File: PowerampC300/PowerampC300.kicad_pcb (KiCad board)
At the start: 2 copper layers, 240 x 63 mm, 110 parts, among them J1 Conn_01x02, J2 Conn_01x02, J3 Conn_01x02, J4 Conn_01x01, J5 Conn_01x01, J6 Conn_01x01, J7 Conn_01x01, J8 Conn_01x02, J9 Conn_Coaxial, Q1 2N5551, Q10 MJE15033, Q11 MJE15032, Q12 MJE15032, Q13 2N5551, Q14 2N5401, Q15 MJE15032, Q16 MJE15033, Q17 MJL3281A, Q18 MJL1302A, Q19 MJL3281A, Q2 2N5551, Q20 MJL1302A, Q21 MJL3281A, Q22 MJL1302A, Q23 MJL3281A, Q24 MJL1302A, Q3 2N5401, Q4 2N5401, Q5 2N5551, Q6 2N5551, Q7 2N5551, Q8 2N5401

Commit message: Added instructions
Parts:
- moved R24 21.4 mm to (186.2, 76.2)
- moved R12 13.5 mm to (188.8, 68.8)
- moved C5 13.5 mm to (196.4, 74.8), turned to 180 degrees
- moved R28 11.1 mm to (182.6, 69.2)
- moved C22 10.8 mm to (193.4, 70.4), turned to 0 degrees
- moved Q14 10.6 mm to (163.2, 68.8)
- moved C13 5.90 mm to (84.8, 68.6)
- moved Q7 5.77 mm to (186.8, 85.6), turned to 180 degrees
- moved Q3 5.30 mm to (101.2, 84.6), turned to 180 degrees
- moved Q4 4.72 mm to (86.8, 84.8), turned to 0 degrees
- moved R27 4.57 mm to (186.2, 73.0)
- moved R4 4.20 mm to (91.8, 75.8)
- moved Q10 3.91 mm to (123.5, 81.8)
- moved D3 3.41 mm to (145.4, 69.0)
- moved R3 3.20 mm to (96.6, 75.8)
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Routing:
- net Net-(D4-Pad2): track 19.2 -> 4.45 mm
- net -48V: track 300.6 -> 287.5 mm
- net Net-(C3-Pad2): track 41.2 -> 30.5 mm
- net Net-(C22-Pad1): track 44.8 -> 53.8 mm
- net Net-(C6-Pad2): track 519.5 -> 526.6 mm
- net Net-(Q12-Pad3): track 11.2 -> 18.1 mm
- net Net-(Q11-Pad1): track 15.7 -> 22.0 mm
- net Net-(Q14-Pad2): track 24.5 -> 30.8 mm
- net Net-(Q3-Pad1): track 4.50 -> 10.7 mm
- net Net-(Q7-Pad3): track 5.07 -> 11.0 mm
- net Net-(D3-Pad1): track 9.05 -> 3.16 mm
- net Net-(Q13-Pad2): track 15.5 -> 21.1 mm
- net Net-(Q7-Pad1): track 5.19 -> 10.1 mm
- net Net-(Q10-Pad3): track 15.4 -> 12.8 mm
- net Net-(C6-Pad1): track 48.5 -> 46.3 mm
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
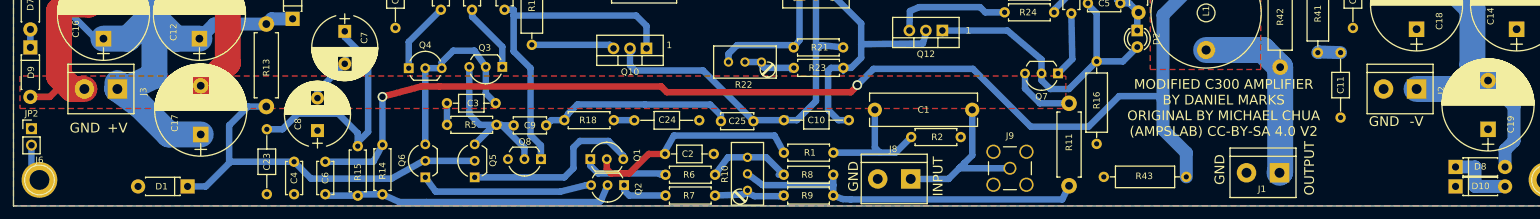
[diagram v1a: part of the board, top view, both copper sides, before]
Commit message: Added option for spade terminal power connections
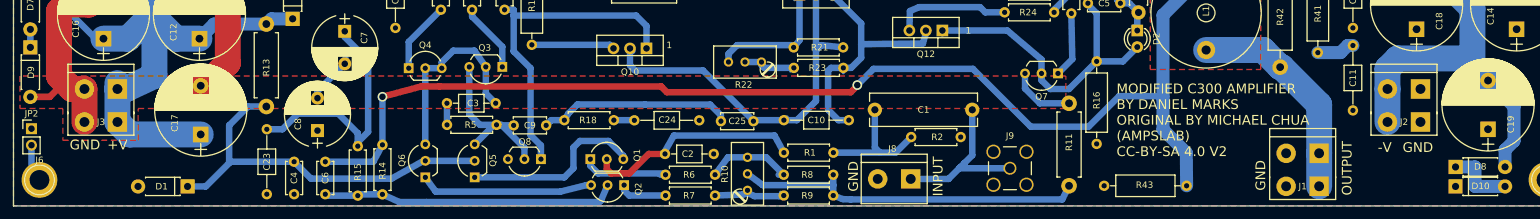
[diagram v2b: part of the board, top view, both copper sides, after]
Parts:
- J1, J2, J3: footprint Connectors_Terminal_Blocks:TerminalBlock_bornier-2_P5.08mm -> poweramp:TerminalBlock_bornier-2_P5.08mm_with_spade
- moved J1 6.80 mm to (227.0, 97.9)
- moved C11 2.20 mm to (232.2, 91.3)
- moved R43 1.37 mm to (193.9, 102.9)
- moved J2 0.60 mm to (242.6, 88.0)
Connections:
- J2 pad 1: -48V -> GND
- J2 pad 2: GND -> -48V
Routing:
- net -48V: track 287.5 -> 298.3 mm
- net GND: track 52.5 -> 57.5 mm
- net OUTPUT: track 28.8 -> 33.5 mm
- net +48V: track 307.5 -> 310.7 mm
- net Net-(C11-Pad2): track 3.54 -> 5.86 mm
- net Net-(C6-Pad2): track 526.6 -> 528.0 mm

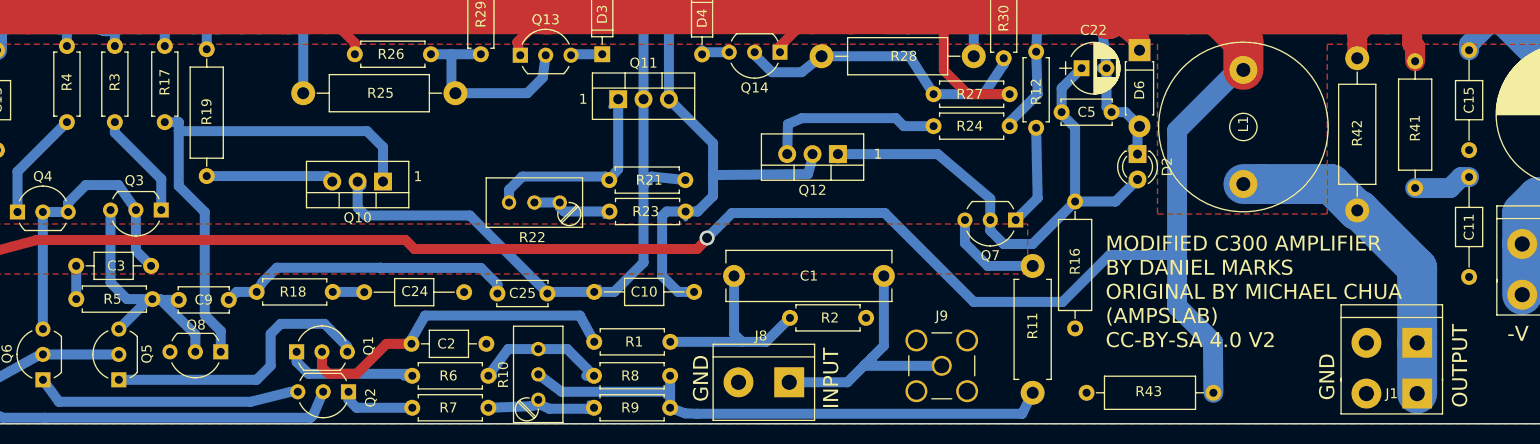
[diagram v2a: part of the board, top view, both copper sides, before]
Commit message: Added OITPC compensation
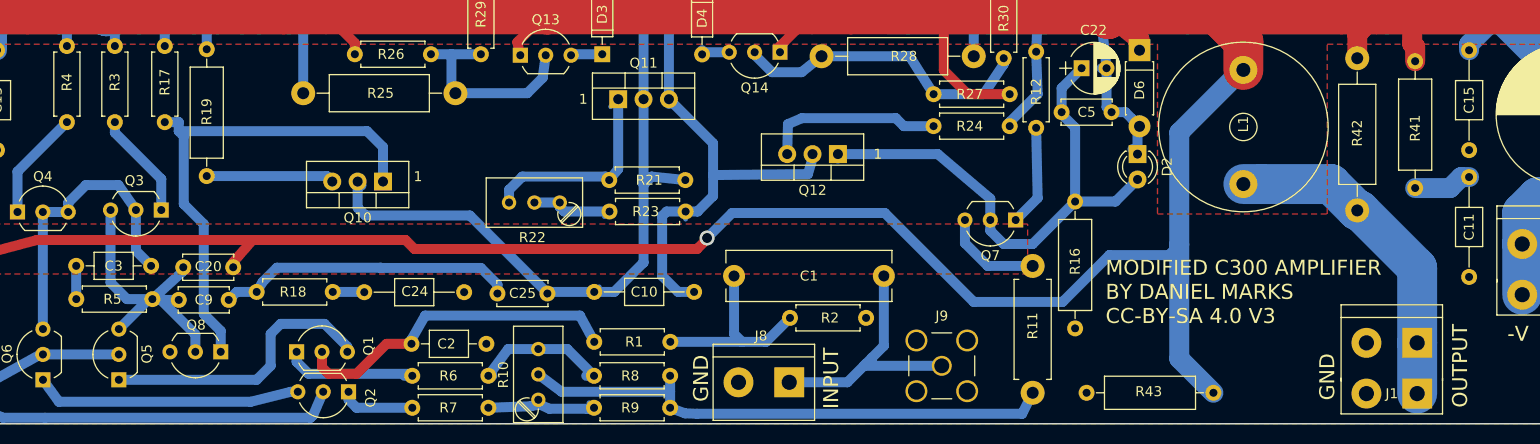
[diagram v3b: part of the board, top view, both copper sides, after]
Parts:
- added C20: NC, Capacitors_THT:C_Disc_D5.0mm_W2.5mm_P5.00mm, F.Cu at (103.5, 90.3)
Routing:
- net Net-(C20-Pad1): track 27.1 -> 31.7 mm
- net Net-(C20-Pad2): track 528.0 -> 532.3 mm
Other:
- board text added: "MODIFIED C300 AMPLIFIER BY DANIEL MARKS CC-BY-SA 4.0 V3"
- board text removed: "MODIFIED C300 AMPLIFIER BY DANIEL MARKS ORIGINAL BY MICHAEL CHUA (AMPSLAB) CC-BY-SA 4.0 V2"

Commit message: Redid star scheme again, added grounding diagram, modified drill template
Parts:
- added D11: 1N4148, Diodes_THT:D_DO-35_SOD27_P7.62mm_Horizontal, F.Cu at (196.2, 104.6)
- added D12: 1N4148, Diodes_THT:D_DO-35_SOD27_P7.62mm_Horizontal, F.Cu at (204.0, 101.8)
- added R20: 10R, Resistors_THT:R_Axial_DIN0207_L6.3mm_D2.5mm_P7.62mm_Horizontal, F.Cu at (196.2, 99.2)
- moved C6 36.6 mm to (110.6, 104.6)
- moved C23 32.4 mm to (97.3, 101.8)
- moved C3 27.1 mm to (70.0, 105.0), turned to 90 degrees
- moved C8 27.0 mm to (99.0, 88.0)
- moved C13 25.2 mm to (110.0, 69.0), turned to 0 degrees
- moved R15 25.0 mm to (104.0, 97.0)
- moved R14 24.6 mm to (107.4, 97.0)
- moved R43 23.6 mm to (216.4, 95.8), turned to 180 degrees
- moved R18 22.7 mm to (133.0, 88.0)
- moved Q8 20.9 mm to (90.3, 86.5), turned to 270 degrees
- moved R5 20.7 mm to (79.7, 95.2), turned to 270 degrees
- moved R17 19.9 mm to (81.8, 76.1)
- moved C25 19.7 mm to (133.6, 73.3), turned to 180 degrees
- moved C24 19.5 mm to (141.0, 91.0), turned to 180 degrees
- moved R3 18.4 mm to (78.2, 76.1)
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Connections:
- C2 pad 1: GND -> GNDS
- C23 pad 1: GND -> GNDS
- C24 pad 2: GND -> GNDS
- C4 pad 1: GND -> GNDS
- C8 pad 1: GND -> GNDS
- D1 pad 2: GND -> GNDS
- J8 pad 2: GND -> GNDS
- J9 pad 2: GND -> GNDS
- JP2 pad 1: GND -> GNDS
- Q8 pad 3: GND -> GNDS
- R16 pad 2: GND -> GNDS
- R2 pad 2: GND -> GNDS
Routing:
- net Net-(C20-Pad2): track 532.3 -> 489.2 mm, vias 2 -> 0
- net GNDS: track 0.00 -> 37.1 mm
- net Net-(C6-Pad1): track 46.3 -> 16.7 mm
- net Net-(Q2-Pad3): track 26.8 -> 50.9 mm
- net Net-(C20-Pad1): track 31.7 -> 53.7 mm
- net Net-(Q1-Pad3): track 29.3 -> 47.7 mm
- net Net-(Q10-Pad1): track 50.7 -> 66.7 mm
- net Net-(C25-Pad1): track 30.0 -> 45.1 mm
- net Net-(Q10-Pad3): track 12.8 -> 23.4 mm
- net Net-(C1-Pad1): track 19.9 -> 10.5 mm
- net Net-(C22-Pad1): track 53.8 -> 62.8 mm
- net Net-(C10-Pad1): track 71.9 -> 63.3 mm
- net Net-(C3-Pad1): track 3.72 -> 11.1 mm
- net INPUT: track 27.9 -> 21.0 mm
- net +48V: track 310.7 -> 316.0 mm
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- added copper zone on F.Cu, net GNDS

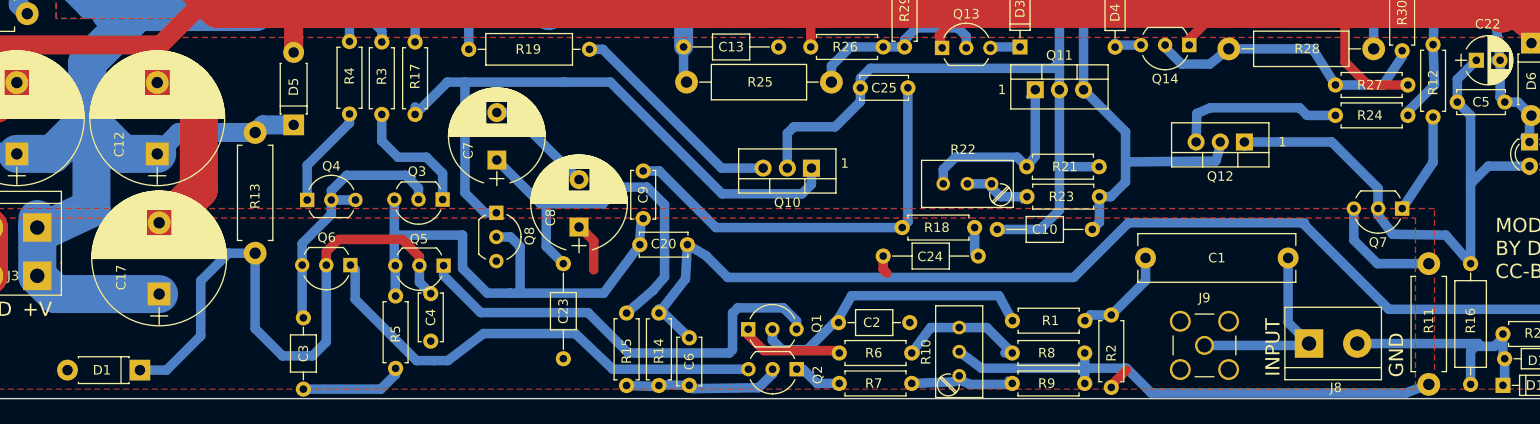
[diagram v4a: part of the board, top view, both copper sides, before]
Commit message: Changed components for lower quiescent power
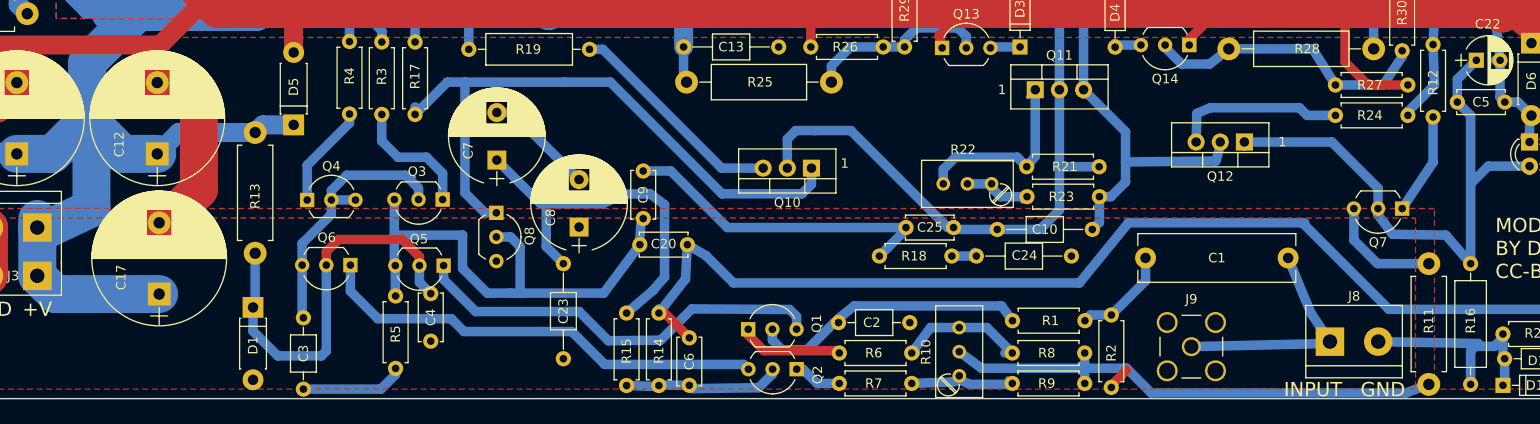
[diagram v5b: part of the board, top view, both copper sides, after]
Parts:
- moved C25 14.7 mm to (133.4, 88.0), turned to 0 degrees
- moved D1 13.6 mm to (64.7, 96.4), turned to 270 degrees
- moved R18 3.84 mm to (130.6, 91.0)
- moved J8 2.21 mm to (178.0, 100.0)
- moved J9 1.39 mm to (163.4, 100.5)
- moved C24 0.20 mm to (140.8, 91.0), turned to 0 degrees
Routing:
- net Net-(C4-Pad2): track 62.9 -> 43.3 mm
- net Net-(C25-Pad1): track 45.1 -> 34.3 mm
- net GNDS: track 37.1 -> 27.8 mm
- net Net-(C10-Pad2): track 93.7 -> 86.7 mm
- net INPUT: track 21.0 -> 24.5 mm
- net Net-(Q1-Pad3): track 47.7 -> 44.3 mm
- net Net-(Q2-Pad3): track 50.9 -> 48.8 mm
- net Net-(C2-Pad2): track 32.7 -> 31.0 mm
- net Net-(C20-Pad2): track 489.2 -> 490.6 mm
- net Net-(C23-Pad2): track 41.2 -> 40.3 mm

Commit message: Added base stopper resistors
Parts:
- added C21: 10 uF, Capacitors_THT:C_Disc_D5.0mm_W2.5mm_P5.00mm, F.Cu at (153.5, 87.8)
- added R44: 2R2, Resistors_THT:R_Axial_DIN0411_L9.9mm_D3.6mm_P15.24mm_Horizontal, F.Cu at (130.3, 55.5)
- added R45: 2R2, Resistors_THT:R_Axial_DIN0411_L9.9mm_D3.6mm_P15.24mm_Horizontal, F.Cu at (107.3, 55.4)
- added R46: 2R2, Resistors_THT:R_Axial_DIN0411_L9.9mm_D3.6mm_P15.24mm_Horizontal, F.Cu at (80.2, 55.2)
- added R47: 2R2, Resistors_THT:R_Axial_DIN0411_L9.9mm_D3.6mm_P15.24mm_Horizontal, F.Cu at (55.2, 55.3)
- added R48: 2R2, Resistors_THT:R_Axial_DIN0411_L9.9mm_D3.6mm_P15.24mm_Horizontal, F.Cu at (226.7, 55.0)
- added R49: 2R2, Resistors_THT:R_Axial_DIN0411_L9.9mm_D3.6mm_P15.24mm_Horizontal, F.Cu at (201.7, 55.0)
- added R50: 2R2, Resistors_THT:R_Axial_DIN0411_L9.9mm_D3.6mm_P15.24mm_Horizontal, F.Cu at (176.8, 55.2)
- added R51: 2R2, Resistors_THT:R_Axial_DIN0411_L9.9mm_D3.6mm_P15.24mm_Horizontal, F.Cu at (151.8, 55.3)
- R24: value 56R -> 120R
- R25, R28: value 3k3 -> 6k8
- moved C10 29.2 mm to (153.2, 59.0)
- moved Q17 2.80 mm to (40.0, 47.2)
- moved Q18 2.80 mm to (242.0, 47.2)
- moved Q19 2.80 mm to (65.0, 47.2)
- moved Q20 2.80 mm to (217.0, 47.2)
- moved Q21 2.80 mm to (90.0, 47.2)
- moved Q22 2.80 mm to (192.0, 47.2)
- moved Q23 2.80 mm to (115.0, 47.2)
- moved Q24 2.80 mm to (167.0, 47.2)
- moved R39 1.71 mm to (109.2, 60.7)
- moved R35 1.70 mm to (55.0, 60.7)
- moved R37 1.67 mm to (82.2, 60.6)
- moved R33 1.65 mm to (27.7, 60.6)
- moved R34 1.40 mm to (263.9, 60.4)
- moved R40 1.30 mm to (182.3, 60.5)
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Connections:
- Q17 pad 1: Net-(Q15-Pad3) -> Net-(Q17-Pad1)
- Q18 pad 1: Net-(Q16-Pad3) -> Net-(Q18-Pad1)
- Q19 pad 1: Net-(Q15-Pad3) -> Net-(Q19-Pad1)
- Q20 pad 1: Net-(Q16-Pad3) -> Net-(Q20-Pad1)
- Q21 pad 1: Net-(Q15-Pad3) -> Net-(Q21-Pad1)
- Q22 pad 1: Net-(Q16-Pad3) -> Net-(Q22-Pad1)
- Q23 pad 1: Net-(Q15-Pad3) -> Net-(Q23-Pad1)
- Q24 pad 1: Net-(Q16-Pad3) -> Net-(Q24-Pad1)
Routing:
- net Net-(Q15-Pad3): track 159.5 -> 131.3 mm
- net +48V: track 316.0 -> 334.8 mm
- net Net-(Q16-Pad3): track 153.8 -> 139.8 mm
- net Net-(Q19-Pad1): track 0.00 -> 13.6 mm
- net Net-(Q21-Pad1): track 0.00 -> 12.2 mm
- net Net-(C10-Pad2): track 86.7 -> 98.6 mm
- net Net-(Q17-Pad1): track 0.00 -> 11.9 mm
- net Net-(Q23-Pad1): track 0.00 -> 10.9 mm
- net Net-(Q24-Pad1): track 0.00 -> 10.7 mm
- net Net-(Q22-Pad1): track 0.00 -> 10.6 mm
- net Net-(Q20-Pad1): track 0.00 -> 10.4 mm
- net Net-(Q18-Pad1): track 0.00 -> 10.3 mm
- net Net-(C10-Pad1): track 63.3 -> 72.1 mm
- net -48V: track 298.3 -> 303.1 mm
- net Net-(Q19-Pad3): track 13.8 -> 17.2 mm
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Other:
- board text added: "MODIFIED C300 AMPLIFIER BY DANIEL MARKS CC-BY-SA 4.0 V4"
- board text removed: "MODIFIED C300 AMPLIFIER BY DANIEL MARKS CC-BY-SA 4.0 V3"

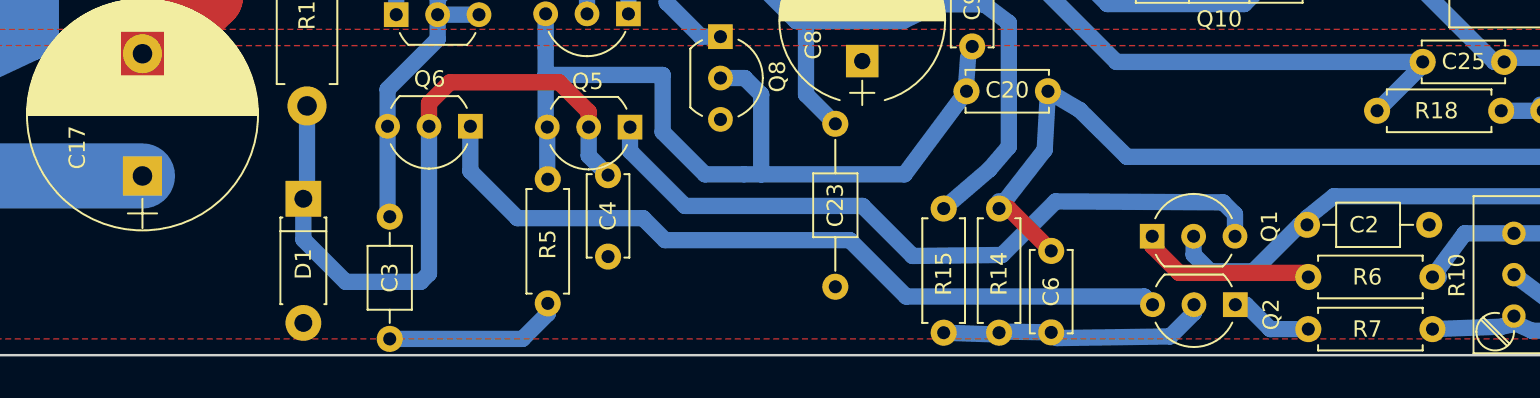
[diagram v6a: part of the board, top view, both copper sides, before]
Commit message: Additions of optional zener diodes to limit current surges
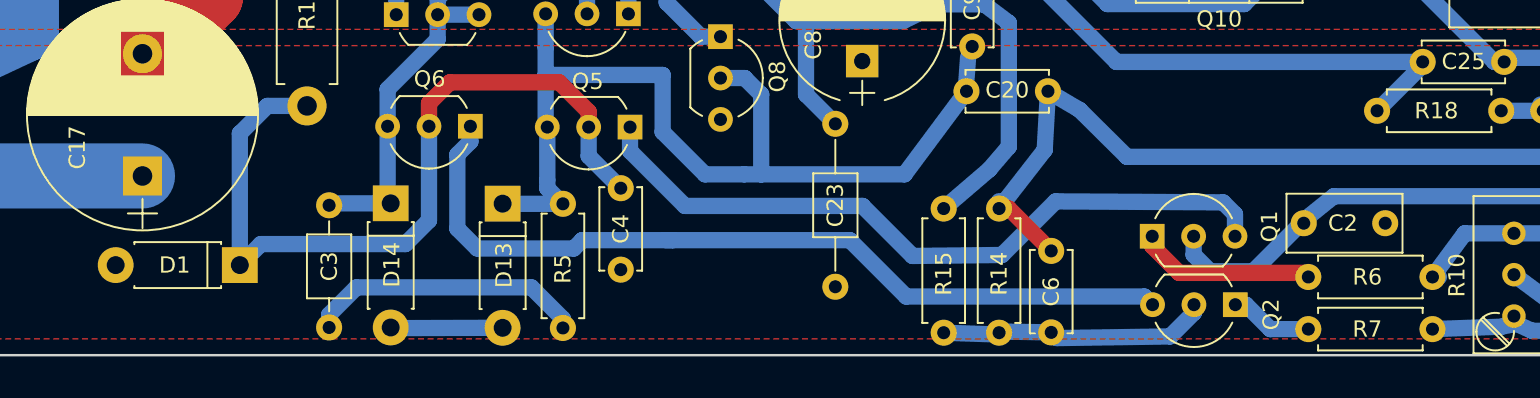
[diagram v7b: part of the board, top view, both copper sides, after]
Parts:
- added D13: NC, Diodes_THT:D_DO-41_SOD81_P7.62mm_Horizontal, F.Cu at (76.9, 96.7)
- added D14: NC, Diodes_THT:D_DO-41_SOD81_P7.62mm_Horizontal, F.Cu at (70.1, 96.7)
- C2: footprint Capacitors_THT:C_Axial_L3.8mm_D2.6mm_P7.50mm_Horizontal -> Capacitors_THT:C_Rect_L7.0mm_W3.5mm_P5.00mm
- R44, R45, R46, R47, R48, R49, R50, R51: value 2R2 -> 1R
- moved D1 5.64 mm to (60.8, 100.5), turned to 180 degrees
- moved C3 3.79 mm to (66.3, 104.3)
- moved C2 2.70 mm to (131.1, 97.9)
- moved R5 1.77 mm to (80.6, 96.7)
- moved C4 1.12 mm to (84.2, 100.8)
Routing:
- net Net-(C4-Pad2): track 43.3 -> 50.2 mm
- net Net-(D13-Pad2): track 0.00 -> 6.89 mm
- net Net-(C3-Pad1): track 11.1 -> 17.3 mm
- net Net-(C20-Pad1): track 53.7 -> 59.3 mm
- net Net-(Q2-Pad3): track 48.8 -> 52.9 mm
- net Net-(C3-Pad2): track 28.8 -> 31.9 mm
